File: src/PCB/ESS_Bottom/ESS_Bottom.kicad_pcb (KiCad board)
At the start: 2 copper layers, 70.8 x 51.4 mm, 14 parts, among them J10 Conn_01x01, J11 Conn_01x01, J12 Conn_01x01, J5 Conn_01x01, J6 Conn_01x01, J7 Conn_01x01, J8 Conn_01x01, J9 Conn_01x01, SW1 SW_Slide_DPDT, U3 ESP32-C3-DevKitM-1

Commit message: added ground fill
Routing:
- added copper zone on B.Cu, net GND
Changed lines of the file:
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@@
 		(net 28)
+	)
+	(zone
+		(net 2)
+		(net_name "GND")
+		(layer "B.Cu")
+		(hatch edge 0.5)
+		(connect_pads
+			(clearance 0.5)
+		)
+		(min_thickness 0.25)
+		(filled_areas_thickness no)
+		(fill yes
+			(thermal_gap 0.5)
+			(thermal_bridge_width 0.5)
+		)
+		(polygon
+			(pts
+				(xy 115.39 71.24) (xy 115.31 121.08) (xy 183.9 121.08) (xy 184.9 118.69) (xy 184.52 71.01) (xy 115.23 71.47)
+				(xy 115.46 71.78)
+			)
+		)
 	)
 	(group ""

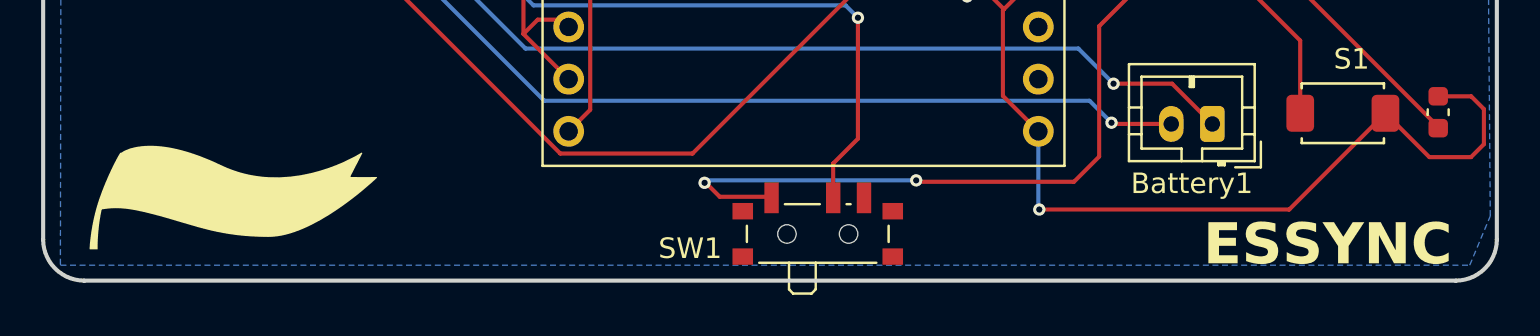
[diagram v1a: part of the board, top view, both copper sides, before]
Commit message: made holes in pcb for mounting
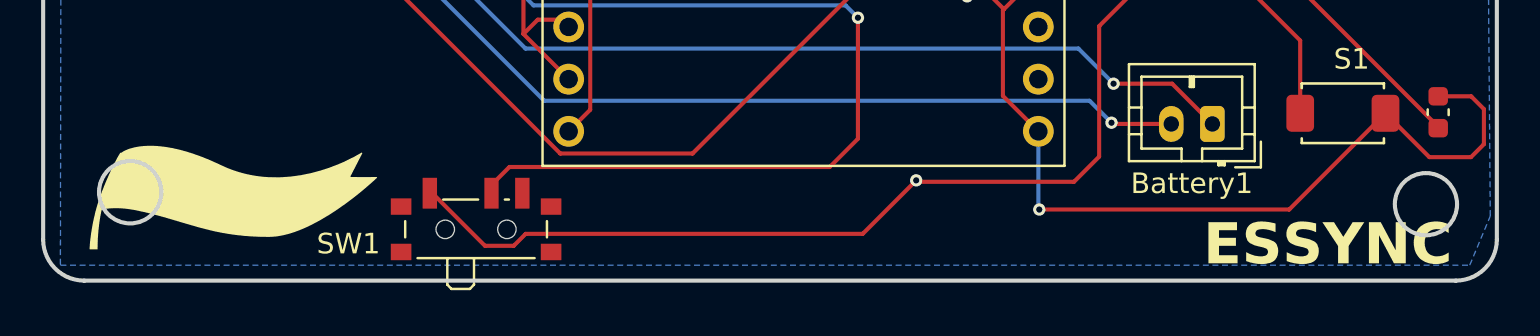
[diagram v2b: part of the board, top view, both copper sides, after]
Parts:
- moved SW1 16.6 mm to (135.5, 119.0)
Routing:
- net /OUT+: track 45.4 -> 61.2 mm
- net /IN+: track 37.1 -> 48.3 mm, vias 2 -> 1
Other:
- outline, holes or cut-outs redrawn
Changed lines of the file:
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@@
 	(footprint "Button_Switch_SMD:SW_SPDT_PCM12"
 		(layer "F.Cu")
-		(at 152.17 119.23)
+		(at 135.54 119.005)
 		(descr "Ultraminiature Surface Mount Slide Switch, right-angle, https://www.ckswitches.com/media/1424/pcm.pdf")
 		(property "Reference" "SW1"
@@
 		(layer "Edge.Cuts")
 	)
+	(gr_circle
+		(center 181.77 118.11)
+		(end 180.69 117.05)
+		(stroke
+			(width 0.2)
+			(type solid)
+		)
+		(fill no)
+		(layer "Edge.Cuts")
+	)
 	(gr_line
 		(start 183.22 121.83)
@@
 		(layer "Edge.Cuts")
 	)
+	(gr_circle
+		(center 118.706626 117.527375)
+		(end 117.19 117.491468)
+		(stroke
+			(width 0.2)
+			(type solid)
+		)
+		(fill no)
+		(layer "Edge.Cuts")
+	)
 	(gr_text "ESSYNC"
 		(at 170.93 121.23 0)
@@
 	)
 	(segment
-		(start 152.92 116.13)
-		(end 152.92 117.8)
+		(start 154.125 114.925)
+		(end 152.75 116.3)
 		(width 0.2)
 		(layer "F.Cu")
@@
 	)
 	(segment
-		(start 154.125 114.925)
-		(end 152.92 116.13)
+		(start 136.29 117.175)
+		(end 136.29 117.575)
 		(width 0.2)
 		(layer "F.Cu")
@@
 		(net 4)
 	)
+	(segment
+		(start 137.165 116.3)
+		(end 136.29 117.175)
+		(width 0.2)
+		(layer "F.Cu")
+		(net 4)
+	)
+	(segment
+		(start 152.75 116.3)
+		(end 137.165 116.3)
+		(width 0.2)
+		(layer "F.Cu")
+		(net 4)
+	)
 	(via
 		(at 136.975 107.075)
@@
 	)
 	(segment
-		(start 168.185 107.125)
-		(end 165.865 109.445)
+		(start 137.371785 120.136)
+		(end 135.973785 120.136)
 		(width 0.2)
 		(layer "F.Cu")
@@
 	)
 	(segment
-		(start 146.66 117.07)
-		(end 146.72 117.07)
+		(start 137.953892 119.553893)
+		(end 137.371785 120.136)
 		(width 0.2)
 		(layer "F.Cu")
@@
 	)
 	(segment
-		(start 149.869 117.749)
-		(end 149.92 117.8)
+		(start 168.185 107.125)
+		(end 165.865 109.445)
 		(width 0.2)
 		(layer "F.Cu")
@@
 	)
 	(segment
-		(start 156.98 117.02)
-		(end 156.98 116.97)
+		(start 135.973785 120.136)
+		(end 133.412785 117.575)
 		(width 0.2)
 		(layer "F.Cu")
@@
 	)
 	(segment
-		(start 164.64 117.02)
-		(end 156.98 117.02)
+		(start 133.412785 117.575)
+		(end 133.29 117.575)
 		(width 0.2)
 		(layer "F.Cu")
@@
 	)
 	(segment
-		(start 149.905 117.215)
-		(end 149.905 118.17)
+		(start 156.98 117.02)
+		(end 156.98 116.97)
 		(width 0.2)
 		(layer "F.Cu")
@@
 	)
 	(segment
-		(start 146.72 117.07)
-		(end 147.399 117.749)
+		(start 164.64 117.02)
+		(end 156.98 117.02)
+		(width 0.2)
+		(layer "F.Cu")
+		(net 5)
+	)
+	(segment
+		(start 156.96 116.95)
+		(end 154.356107 119.553893)
 		(width 0.2)
 		(layer "F.Cu")
@@
 	)
 	(segment
-		(start 147.399 117.749)
-		(end 149.869 117.749)
+		(start 154.356107 119.553893)
+		(end 137.953892 119.553893)
 		(width 0.2)
 		(layer "F.Cu")
@@
 		(net 5)
 	)
-	(via
-		(at 146.66 117.07)
-		(size 0.6)
-		(drill 0.3)
-		(layers "F.Cu" "B.Cu")
-		(net 5)
-	)
-	(segment
-		(start 146.78 116.95)
-		(end 146.66 117.07)
-		(width 0.2)
-		(layer "B.Cu")
-		(net 5)
-	)
-	(segment
-		(start 156.96 116.95)
-		(end 146.78 116.95)
-		(width 0.2)
-		(layer "B.Cu")
-		(net 5)
-	)
